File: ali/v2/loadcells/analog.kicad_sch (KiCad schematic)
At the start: 57 parts, among them J10 Conn_01x04, J11 Conn_01x04, J12 Conn_01x04, J13 Conn_01x04, J14 Conn_01x04, J9 Conn_01x04, U5 ADS124S08

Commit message: mfw tcs
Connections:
- net GND: now also U5.17 (CLK)
- no-connect marks 1 -> 0
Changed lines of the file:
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@@
 		(color 0 0 0 0)
 	)
-	(no_connect
-		(at 227.33 106.68)
-	)
 	(wire
 		(pts
@@
 	(wire
 		(pts
+			(xy 228.6 107.95) (xy 228.6 106.68)
+		)
+		(stroke
+			(width 0)
+			(type default)
+		)
+	)
+	(wire
+		(pts
 			(xy 107.95 73.66) (xy 107.95 74.93)
 		)
@@
 	(wire
 		(pts
+			(xy 228.6 106.68) (xy 227.33 106.68)
+		)
+		(stroke
+			(width 0)
+			(type default)
+		)
+	)
+	(wire
+		(pts
 			(xy 60.96 63.5) (xy 60.96 62.23)
 		)
@@
 					(unit 1)
 				)
+			)
+		)
+	)
+	(symbol
+		(lib_id "power:GND")
+		(at 228.6 107.95 0)
+		(unit 1)
+		(body_style 1)
+		(exclude_from_sim no)
+		(in_bom yes)
+		(on_board yes)
+		(in_pos_files yes)
+		(dnp no)
+		(fields_autoplaced yes)
+		(property "Reference" "#PWR097"
+			(at 228.6 114.3 0)
+			(hide yes)
+			(show_name no)
+			(do_not_autoplace no)
+			(effects
+				(font
+					(size 1.27 1.27)
+				)
+			)
+		)
+		(property "Value" "GND"
+			(at 228.6 113.03 0)
+			(hide yes)
+			(show_name no)
+			(do_not_autoplace no)
+			(effects
+				(font
+					(size 1.27 1.27)
+				)
+			)
+		)
+		(property "Footprint" ""
+			(at 228.6 107.95 0)
+			(hide yes)
+			(show_name no)
+			(do_not_autoplace no)
+			(effects
+				(font
+					(size 1.27 1.27)
+				)
+			)
+		)
+		(property "Datasheet" ""
+			(at 228.6 107.95 0)
+			(hide yes)
+			(show_name no)
+			(do_not_autoplace no)
+			(effects
+				(font
+					(size 1.27 1.27)
+				)
+			)
+		)
+		(property "Description" "Power symbol creates a global label with name \"GND\" , ground"
+			(at 228.6 107.95 0)
+			(hide yes)
+			(show_name no)
+			(do_not_autoplace no)
+			(effects
+				(font
+					(size 1.27 1.27)
+				)
+			)
+		)
+		(pin "1"
+		)
+		(instances
+			(project "load-cell"
+				(path "/0eb5ae8a-84ea-4b7e-bec4-bb4e0217d666/de3cef6c-f0bf-43f9-bc77-3e59044b84fe"
+					(reference "#PWR097")
+					(unit 1)
+				)

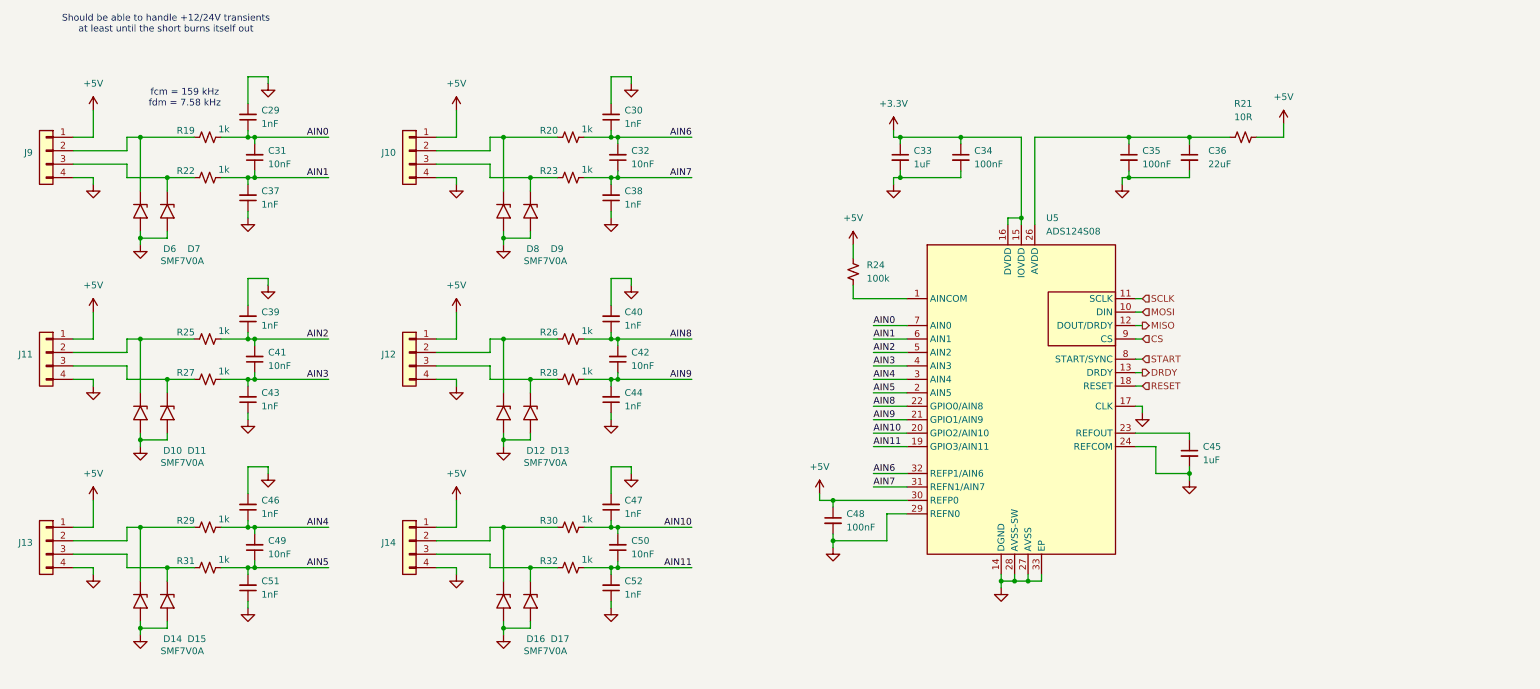
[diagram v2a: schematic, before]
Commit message: Swap to sync'd ADS1261s on LC, update README and clean up Just scripts, some frame changes too.
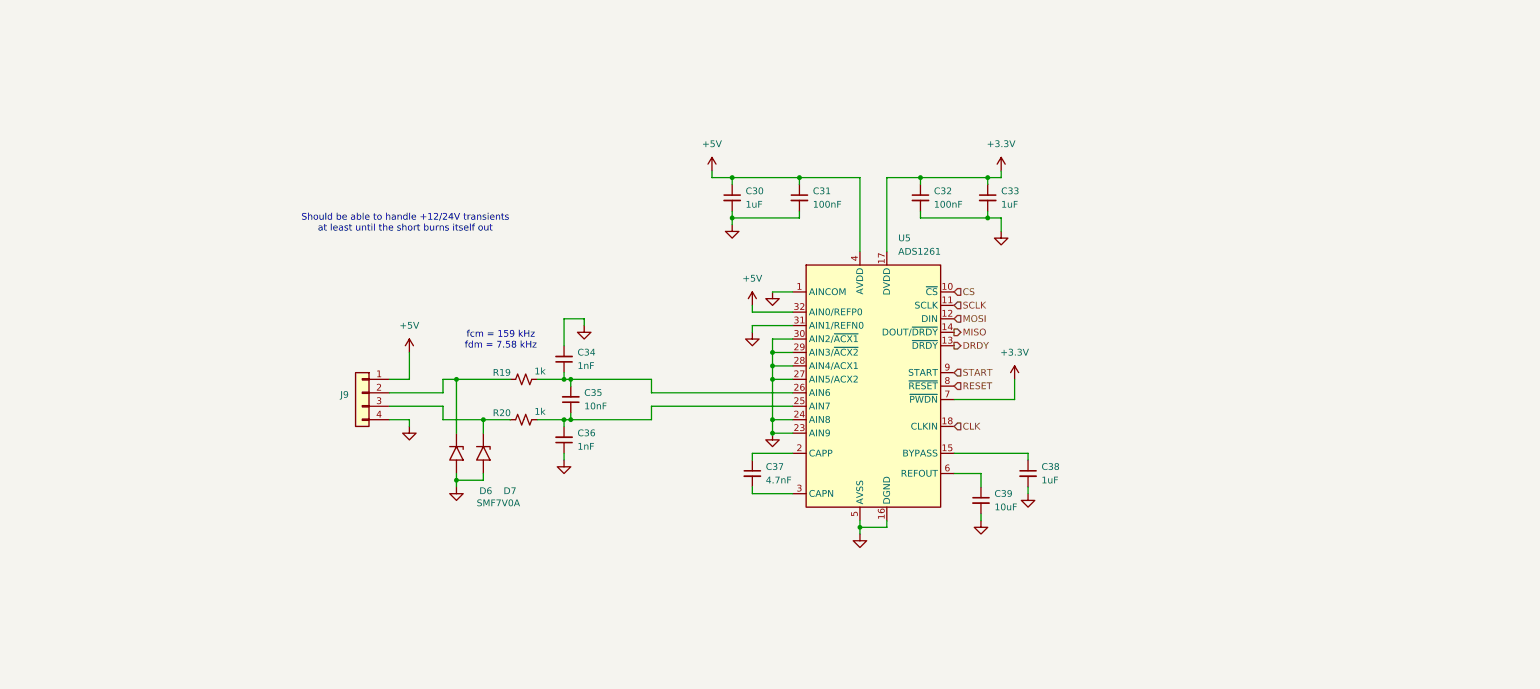
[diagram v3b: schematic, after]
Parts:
- removed C29, C40, C43, C44, C46, C47, C51, C52: 1nF, APRL_Passive:C_0603, symbol Device:C_Small
- removed C41, C42, C49, C50: 10nF, APRL_Passive:C_0603, symbol Device:C_Small
- removed C45: 1uF, APRL_Passive:C_0603, symbol Device:C_Small
- removed C48: 100nF, APRL_Passive:C_0603, symbol Device:C_Small
- removed D10, D11, D12, D13, D14, D15, D16, D17, D8, D9: SMF7V0A, Diode_SMD:D_SMF, symbol Diode:SMF5V0A
- removed J10, J11, J12, J13, J14: Conn_01x04, APRL_Connector_Molex:Molex_CLIK-Mate_503159-0401_1x04-1MP_P1.50mm_Vertical, symbol Connector_Generic:Conn_01x04
- removed R21: 10R, APRL_Passive:R_0603, symbol Device:R_Small_US
- removed R22, R23, R25, R26, R27, R28, R29, R30, R31, R32: 1k, APRL_Passive:R_0603, symbol Device:R_Small_US
- removed R24: 100k, APRL_Passive:R_0603, symbol Device:R_Small_US
- removed U5: ADS124S08, APRL_Package:QFN-32_EP_5.8x5.8_Pitch0.5mm, symbol APRL_Analog:ADS124S08
- added U5: ADS1261, APRL_Package_QFN:Texas_RHB0032E_VQFN-32-1EP_5x5mm_P0.5mm_EP3.45x3.45mm_ThermalVias, symbol APRL_Analog:ADS1261
- C30, C38: value 1nF -> 1uF; MPN GRM21B5C2J102FWA3 -> GRM188D72A105KE01
- C31, C32: value 10nF -> 100nF; MPN GRM21B5C2E103FWAA -> GRM188R72A104KA35
- C34: value 100nF -> 1nF; MPN GRM188R72A104KA35 -> GRM21B5C2J102FWA3
- C35: value 100nF -> 10nF; MPN GRM188R72A104KA35 -> GRM21B5C2E103FWAA
- C36: value 22uF -> 1nF; footprint APRL_Passive:C_0805 -> APRL_Passive:C_0603; MPN GRM21BZ71A226ME15 -> GRM21B5C2J102FWA3
- C37: value 1nF -> 4.7nF; MANUFACTURER Murata -> (none); MPN GRM21B5C2J102FWA3 -> (none)
- C39: value 1nF -> 10uF; MANUFACTURER Murata -> (none); MPN GRM21B5C2J102FWA3 -> (none)
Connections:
- net +3.3V: now also C32.1, U5.17 (DVDD), U5.7 (~{PWDN}); no longer C34.1
- net +5V: now also C30.1, C31.1, U5.32 (AIN0/REFP0), U5.4 (AVDD)
- net CS: now also U5.10 (~{CS})
- net DRDY: now also U5.13 (~{DRDY})
- net GND: now also C31.2, C32.2, C36.1, C38.2, U5.1 (AINCOM), U5.16 (DGND), U5.23 (AIN9), U5.24 (AIN8), U5.27 (AIN5/ACX2), U5.28 (AIN4/ACX1), U5.29 (AIN3/~{ACX2}), U5.30 (AIN2/~{ACX1}), U5.31 (AIN1/REFN0), U5.33 (AVSS), U5.5 (AVSS); no longer C35.2, C36.2, C37.1, C38.1
- net MISO: now also U5.14 (DOUT/~{DRDY})
- net MOSI: now also U5.12 (DIN)
- net RESET: now also U5.8 (~{RESET})
- net SCLK: now also U5.11 (SCLK)
- net START: now also U5.9 (START)
- net at C35.1: now also C36.2, R20.2, U5.25 (AIN7); no longer C36.1
- net at D7.1 (A1), J9.3 (Pin_3): now also R20.1
- net AIN0: no longer names the net of R19.2
- net AIN0: now also C34.1, C35.2, U5.26 (AIN6); no longer C31.2
- net AIN1: no longer names the net of C37.2
- net AIN1: now also U5.3 (CAPN); no longer C31.1
- net AIN2: no longer names the net of C39.1
- net AIN2: now also U5.6 (REFOUT)
- removed net AIN6: C30.1, C32.2, R20.2
- removed net AIN7: C32.1, C38.2
- new net: C38.1, U5.15 (BYPASS)
- new net: U5.19 (NC), U5.20 (NC), U5.21 (NC), U5.22 (NC)
- new net: C37.1, U5.2 (CAPP)
- new net CLK: U5.18 (CLKIN)

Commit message: Minor thermocouple updates
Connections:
- net GND: no longer U5.23 (AIN9), U5.24 (AIN8), U5.27 (AIN5/ACX2), U5.28 (AIN4/ACX1), U5.29 (AIN3/~{ACX2}), U5.30 (AIN2/~{ACX1})
- no-connect marks 0 -> 6

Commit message: Globally remove LCSC labels, update MPNs and IOCs, add +5V monitoring to DAQs, fix some footprints
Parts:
- C34, C36: MPN GRM21B5C2J102FWA3 -> GRM1885C1H102FA01
- C35: MPN GRM21B5C2E103FWAA -> GRM1885C1H103JA01
- C37: MANUFACTURER (none) -> Murata; MPN (none) -> GRM1885C1H472JA01
- C39: MANUFACTURER (none) -> Murata; MPN (none) -> GRM188R61A106KE69
- U5: MANUFACTURER (none) -> TI; MPN (none) -> ADS1261IRHBR
- renumbered R19 to R22, R20 to R23
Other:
- note added: "LOAD CELL INPUT"
- moved on the sheet: C30, C31, C32, C33, C34, C35, C36, C37, C38, C39, D6, D7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

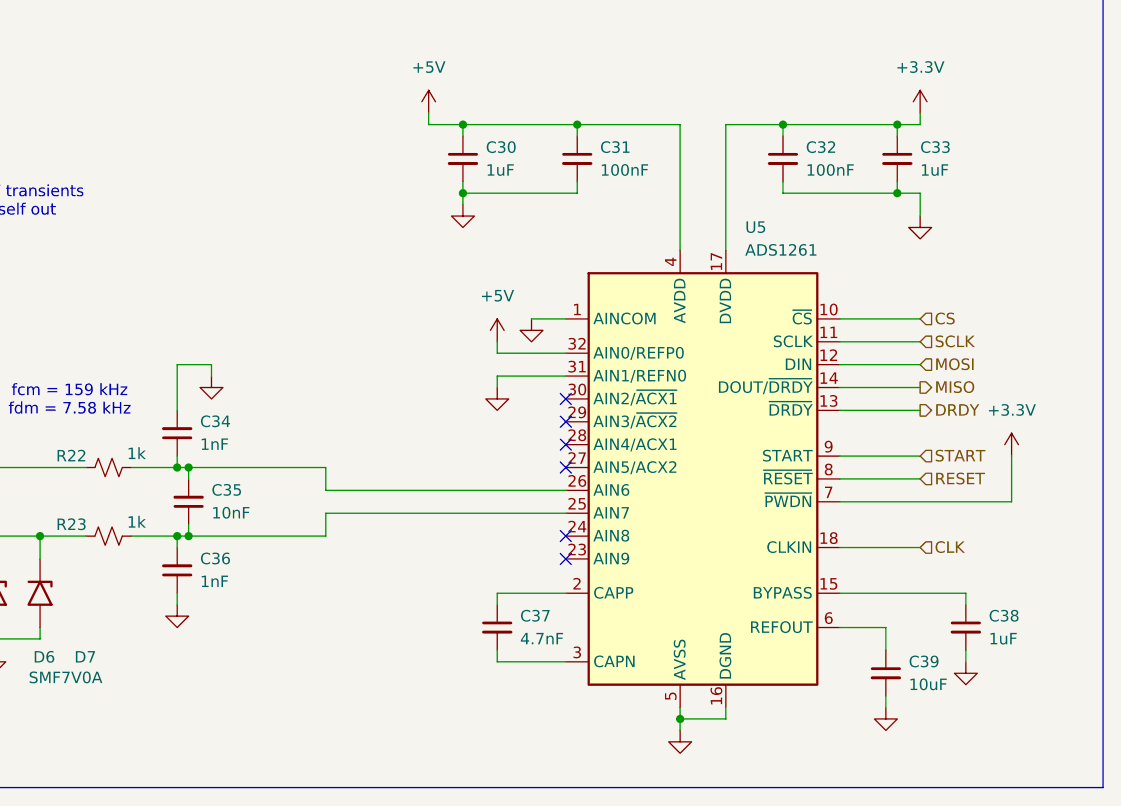
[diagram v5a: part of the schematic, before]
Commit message: the great flatpak and kicad 10.0.6 migration
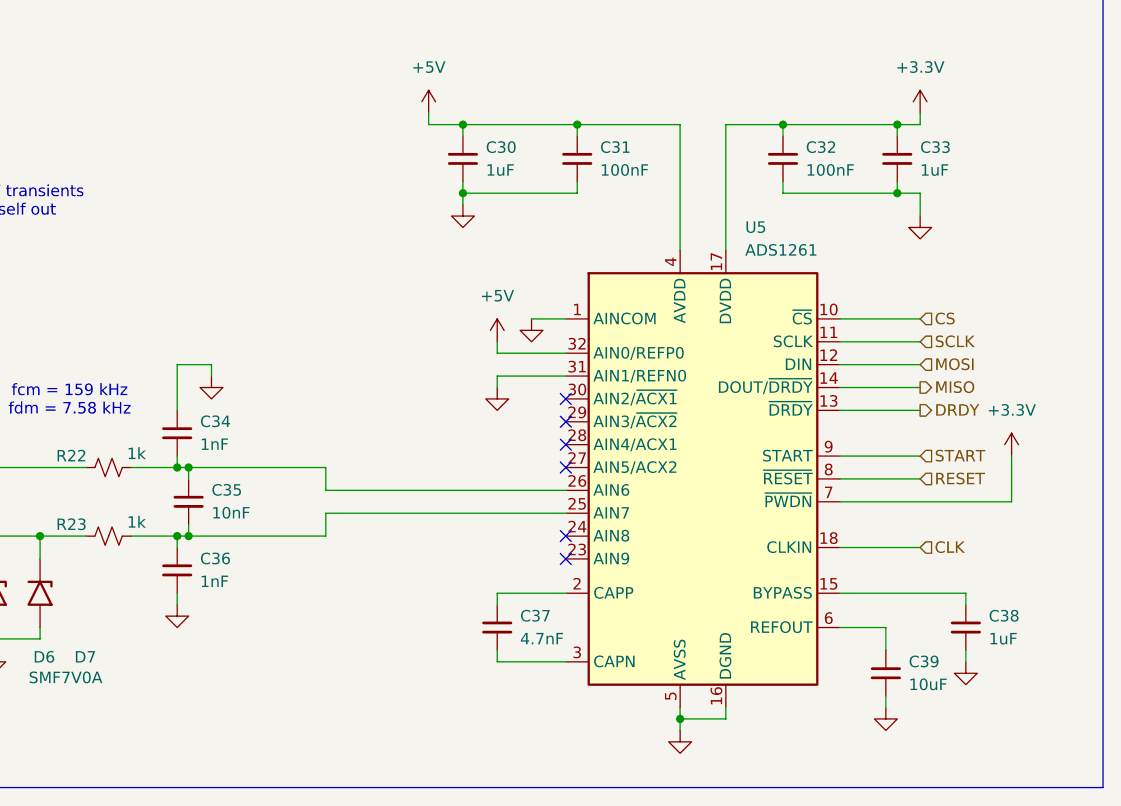
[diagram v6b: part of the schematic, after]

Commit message: Add more commentary
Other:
- note added: "I ended up omitting the RC filter on this thing because it'd mean a mismatch between the voltage range of the load cells and what the chip was capable of. On the off chance that a bridge was ever connected to this thing that did need the full range, I didn't want this to be the limit."
- note added: "I think we will end up sampling at 7200 Hz with a sinc3, which grants a bandwidth of 1750 Hz and a Effective Resolution (Noise-Free Resolution) of 18.8 (15.9)"
- note added: "This chip has AC excitation, and I was thinking about breaking it out, but it yields very little benefit for our application so I just left it out"
- note added: "We could have used a PGA280 to get +10V excitation but I think the temperature rise of the load cells + the increased noise floor would eat any of our precision gains"
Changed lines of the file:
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@@
+		)
+	)
+	(text "This chip has AC excitation, and I was thinking about breaking it out,\nbut it yields very little benefit for our application so I just left it out"
+		(exclude_from_sim no)
+		(at 120.396 86.868 0)
+		(effects
+			(font
+				(size 1.27 1.27)
+			)
+		)
+	)
+	(text "We could have used a PGA280 to get +10V excitation but I think the temperature rise\nof the load cells + the increased noise floor would eat any of our precision gains"
+		(exclude_from_sim no)
+		(at 104.902 155.956 0)
+		(effects
+			(font
+				(size 1.27 1.27)
+			)
+		)
+	)
+	(text "I ended up omitting the RC filter on this thing because it'd mean a mismatch between\nthe voltage range of the load cells and what the chip was capable of. On the off chance\nthat a bridge was ever connected to this thing that did need the full range, I didn't want\nthis to be the limit."
+		(exclude_from_sim no)
+		(at 161.036 53.594 0)
+		(effects
+			(font
+				(size 1.27 1.27)
+			)
 		)
 	)
@@
 		(effects
 			(font
+				(size 1.27 1.27)
+			)
+		)
+	)
+	(text "I think we will end up sampling at 7200 Hz with a sinc3, which grants a bandwidth of 1750 Hz and a Effective Resolution (Noise-Free Resolution) of 18.8 (15.9) "
+		(exclude_from_sim no)
+		(at 138.938 145.796 0)
+		(effects
+			(font

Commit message: Add note on ADC selection
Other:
- note added: "Honestly this chip is overkill and overpriced ($20/chip) for this application. ADS1220 spam ($3/chip) is an infinitely better fit, and due to cost, might be a better choice on the thermocouple board too."
- note removed: "I ended up omitting the RC filter on this thing because it'd mean a mismatch between the voltage range of the load cells and what the chip was capable of. On the off chance that a bridge was ever connected to this thing that did need the full range, I didn't want this to be the limit."
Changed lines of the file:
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@@
 	(text "This chip has AC excitation, and I was thinking about breaking it out,\nbut it yields very little benefit for our application so I just left it out"
 		(exclude_from_sim no)
-		(at 120.396 86.868 0)
+		(at 109.474 86.614 0)
 		(effects
 			(font
@@
 		)
 	)
-	(text "I ended up omitting the RC filter on this thing because it'd mean a mismatch between\nthe voltage range of the load cells and what the chip was capable of. On the off chance\nthat a bridge was ever connected to this thing that did need the full range, I didn't want\nthis to be the limit."
+	(text "Honestly this chip is overkill and overpriced ($20/chip) for this application.\nADS1220 spam ($3/chip) is an infinitely better fit, and due to cost, might\nbe a better choice on the thermocouple board too."
 		(exclude_from_sim no)
-		(at 161.036 53.594 0)
+		(at 255.016 96.52 0)
 		(effects
 			(font
